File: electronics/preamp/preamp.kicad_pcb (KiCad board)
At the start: 2 copper layers, 33 parts, among them J1 Conn_01x01, J2 Conn_01x01, J3 Conn_01x01, J4 Conn_01x01, J5 Conn_01x01, J6 Conn_01x01, J7 Conn_01x01, Q1 BSS138L, U1 TL062, U2 TL062

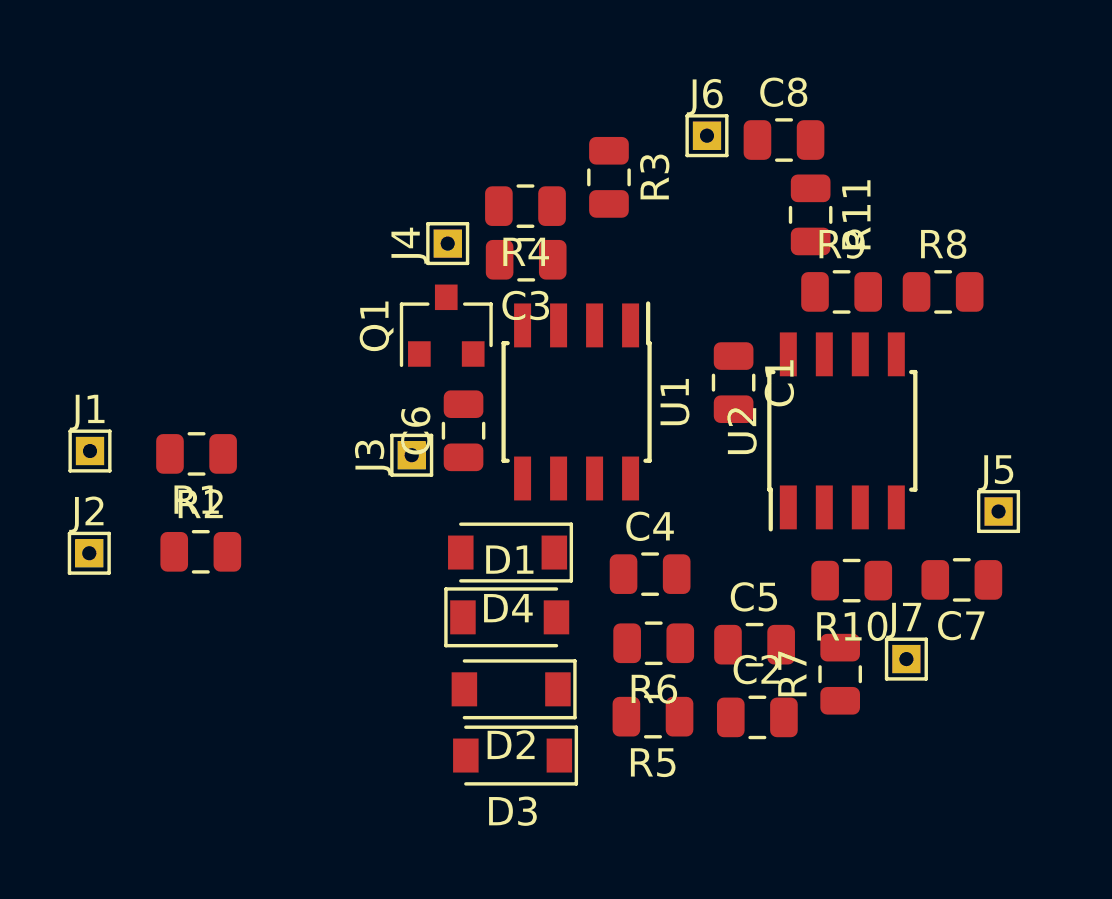
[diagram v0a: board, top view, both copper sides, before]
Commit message: Tweak component placement
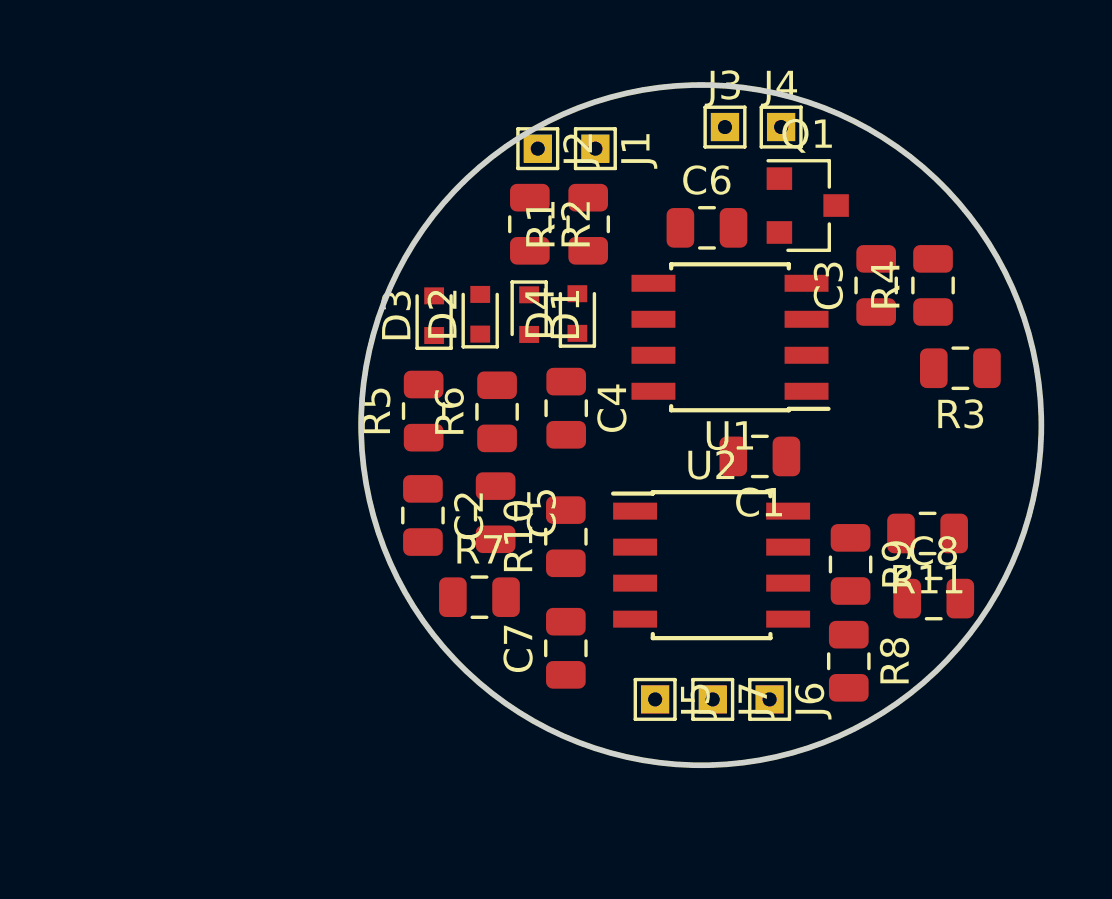
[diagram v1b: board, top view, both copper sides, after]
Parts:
- D1, D2, D3, D4: footprint Diode_SMD:D_SOD-123 -> Diode_SMD:D_SOD-523
- moved J2 21.3 mm to (94.2, 90.2), turned to 270 degrees
- moved J1 20.8 mm to (96.3, 90.2), turned to 270 degrees
- moved J6 20.0 mm to (102.4, 109.7), turned to 270 degrees
- moved C8 17.0 mm to (108.2, 106.1)
- moved R2 16.4 mm to (94.0, 92.9), turned to 270 degrees
- moved R1 16.0 mm to (96.0, 92.9), turned to 90 degrees
- moved J3 16.0 mm to (100.8, 89.5), turned to 0 degrees
- moved D3 15.8 mm to (90.6, 96.1), turned to 90 degrees
- moved R4 14.6 mm to (108.2, 95.1), turned to 90 degrees
- moved C7 14.2 mm to (95.2, 107.9), turned to 90 degrees
- moved R3 14.1 mm to (109.1, 98.0), turned to 180 degrees
- moved J5 13.8 mm to (98.4, 109.7), turned to 270 degrees
- moved C2 13.8 mm to (90.2, 103.2), turned to 270 degrees
- moved R5 13.5 mm to (90.2, 99.5), turned to 90 degrees
- moved R8 13.4 mm to (105.2, 108.3), turned to 270 degrees
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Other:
- board outline added: 24 x 24 mm
- board text added: "IN"
- board text added: "OUT"
- board text added: "PWR"

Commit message: Initial routing
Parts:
- C4: value 220pF -> 4.7pF
- R5: value 2k -> 22k
- R6: value 22k -> 220k
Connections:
- net Net-(R10-Pad2) renamed /BUF+
- net Net-(R11-Pad2) renamed /BUF-
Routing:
- net VGND: track 0.00 -> 52.4 mm, vias 0 -> 2
- net +BATT: track 0.00 -> 33.1 mm, vias 0 -> 2
- net GND: track 0.00 -> 26.9 mm
- net /BUF+: track 0.00 -> 21.0 mm, vias 0 -> 2
- net AMP: track 0.00 -> 20.8 mm, vias 0 -> 2
- net /PRE-: track 0.00 -> 12.9 mm
- net Net-(C4-Pad2): track 0.00 -> 9.68 mm
- net /PRE+: track 0.00 -> 7.73 mm
- net /OUT-: track 0.00 -> 7.35 mm
- net Net-(C3-Pad1): track 0.00 -> 6.56 mm
- net /BUF-: track 0.00 -> 4.18 mm
- net -BATT: track 0.00 -> 4.01 mm
- net Net-(R8-Pad1): track 0.00 -> 3.88 mm
- net /OUT+: track 0.00 -> 3.51 mm
- net Net-(C8-Pad2): track 0.00 -> 2.39 mm
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
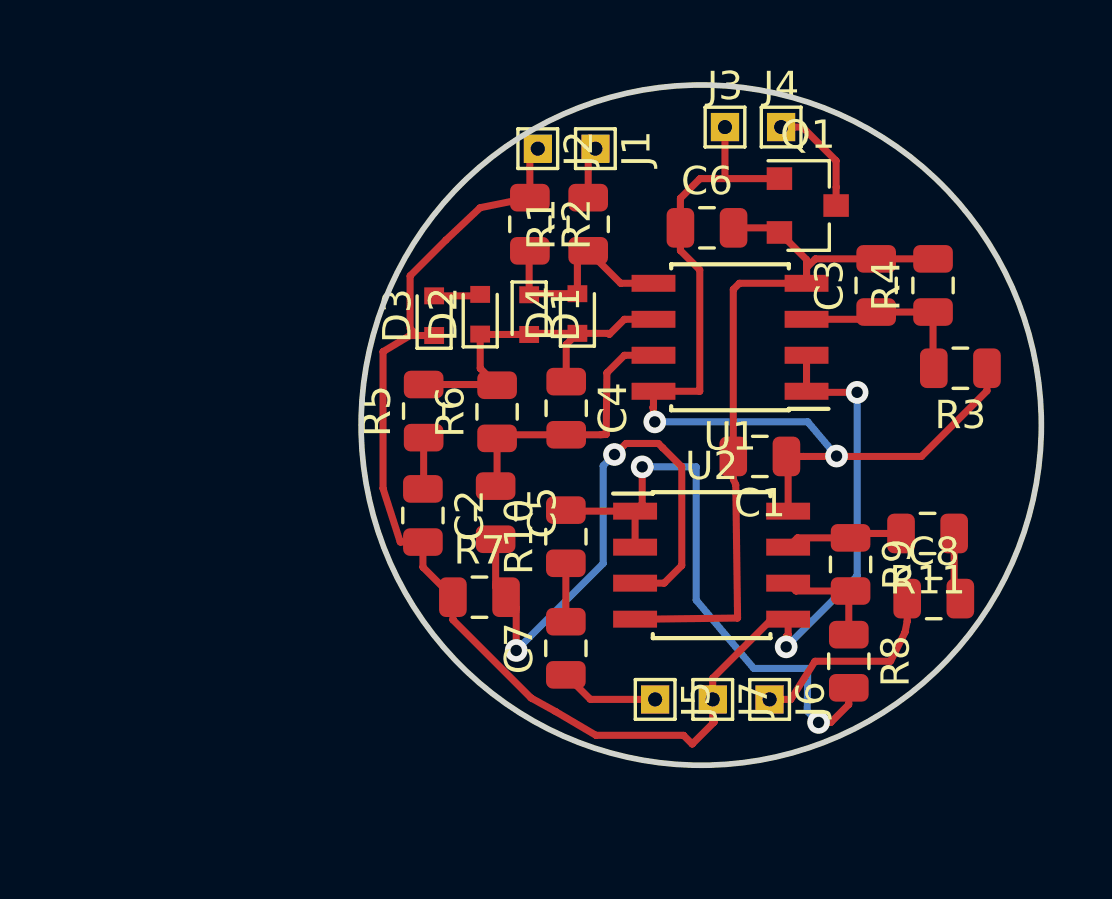
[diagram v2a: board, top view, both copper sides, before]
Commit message: Tweak routing a little bit
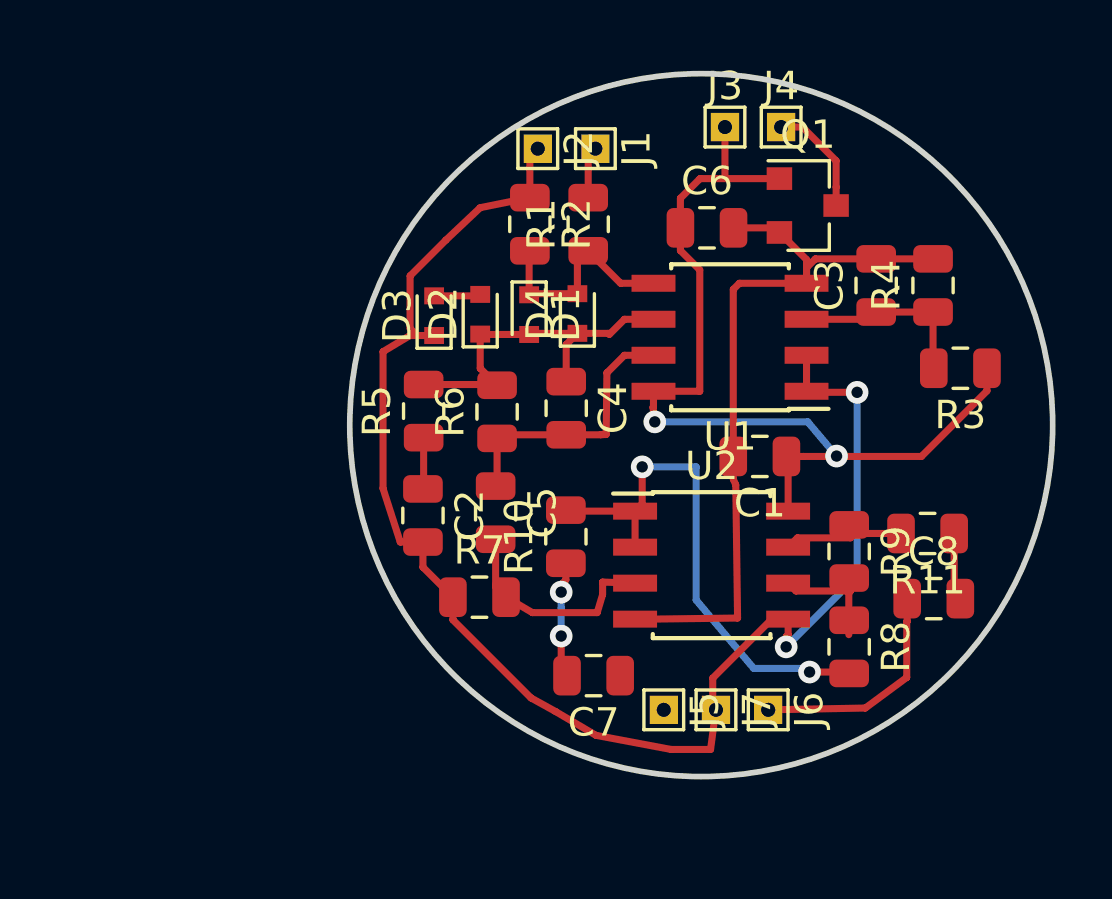
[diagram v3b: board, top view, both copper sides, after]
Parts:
- moved C7 1.37 mm to (96.2, 108.8), turned to 180 degrees
- moved R8 0.51 mm to (105.2, 107.8)
- moved J5 0.48 mm to (98.7, 110.0)
- moved R9 0.46 mm to (105.2, 104.5)
- moved J7 0.39 mm to (100.5, 110.0)
- moved J6 0.37 mm to (102.4, 110.0)
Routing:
- net AMP: track 20.8 -> 7.82 mm, vias 2 -> 0
- net /OUT+: track 3.51 -> 0.00 mm
- net /BUF+: track 21.0 -> 18.5 mm
- net Net-(C7-Pad2): track 2.06 -> 4.12 mm, vias 0 -> 2
- net /OUT-: track 7.35 -> 8.03 mm
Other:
- board size 24 x 24 mm -> 24.8 x 24.8 mm

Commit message: Ready to make first proto
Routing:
- net /OUT+: track 0.00 -> 2.04 mm
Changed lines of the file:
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@@
     (thickness 1.6)
     (drawings 4)
-    (tracks 165)
+    (tracks 166)
     (zones 0)
     (modules 33)
@@
     (tags SOT-23)
     (attr smd)
-    (fp_text reference Q1 (at 0 -2.5) (layer F.SilkS)
+    (fp_text reference Q1 (at 2.8575 -0.9398) (layer F.SilkS)
       (effects (font (size 1 1) (thickness 0.15)))
     )
@@
     (pad 1 smd roundrect (at -0.9375 0 90) (size 0.975 1.4) (layers F.Cu F.Paste F.Mask) (roundrect_rratio 0.25)
       (net 17 /PRE+))
-    (model ${KISYS3DMOD}/Resistor_SMD.3dshapes/R_0805_2012Metric.wrl
+    (model ${KISYS3DMOD}/Resistors_SMD.3dshapes/R_0805.wrl
       (at (xyz 0 0 0))
       (scale (xyz 1 1 1))
@@
     (tags "test point THT pad rectangle square")
     (attr virtual)
-    (fp_text reference J3 (at 0 -1.448) (layer F.SilkS)
+    (fp_text reference J3 (at -2.032 -0.2667) (layer F.SilkS)
       (effects (font (size 1 1) (thickness 0.15)))
     )
@@
     (tags "test point THT pad rectangle square")
     (attr virtual)
-    (fp_text reference J4 (at 0 -1.448) (layer F.SilkS)
+    (fp_text reference J4 (at 2.0828 -0.1397) (layer F.SilkS)
       (effects (font (size 1 1) (thickness 0.15)))
     )
@@
     )
   )
-  (gr_text OUT (at 104.4448 113.665) (layer Eco1.User)
+  (gr_text OUT (at 100.9015 112.5855) (layer Eco1.User)
     (effects (font (size 1.5 1.5) (thickness 0.3)))
   )
-  (gr_text PWR (at 106.0704 87.0712) (layer Eco1.User)
+  (gr_text PWR (at 102.235 86.36) (layer Eco1.User)
     (effects (font (size 1.5 1.5) (thickness 0.3)))
   )
-  (gr_text IN (at 90.9828 87.7316) (layer Eco1.User)
+  (gr_text IN (at 94.996 87.757) (layer Eco1.User)
     (effects (font (size 1.5 1.5) (thickness 0.3)))
   )
@@
   (segment (start 97.666657 105.575618) (end 96.52 105.537) (width 0.25) (layer F.Cu) (net 7))
   (segment (start 96.52 105.537) (end 96.52 105.9815) (width 0.25) (layer F.Cu) (net 7))
+  (segment (start 98.3465 110.0455) (end 97.14 108.839) (width 0.25) (layer F.Cu) (net 8))
+  (segment (start 98.679 110.0455) (end 98.3465 110.0455) (width 0.25) (layer F.Cu) (net 8))
   (segment (start 95.2246 105.4618) (end 95.0595 105.6269) (width 0.25) (layer F.Cu) (net 9))
   (segment (start 95.2246 104.8743) (end 95.2246 105.4618) (width 0.25) (layer F.Cu) (net 9))
@@
   (segment (start 104.759 91.6028) (end 104.759 92.2528) (width 0.25) (layer F.Cu) (net 14))
   (segment (start 102.8192 89.4842) (end 103.5692 89.4842) (width 0.25) (layer F.Cu) (net 14))
-  (segment (start 103.343757 105.852718) (end 103.066657 105.575618) (width 0.25) (layer F.Cu) (net 15))
-  (segment (start 105.268857 105.852718) (end 103.343757 105.852718) (width 0.25) (layer F.Cu) (net 15))
-  (segment (start 105.2068 105.914775) (end 105.268857 105.852718) (width 0.25) (layer F.Cu) (net 15))
-  (segment (start 105.2068 107.3935) (end 105.2068 105.914775) (width 0.25) (layer F.Cu) (net 15))
+  (segment (start 105.2195 106.8855) (end 105.2195 105.395) (width 0.25) (layer F.Cu) (net 15))
+  (segment (start 103.247275 105.395) (end 103.066657 105.575618) (width 0.25) (layer F.Cu) (net 15))
+  (segment (start 105.2195 105.395) (end 103.247275 105.395) (width 0.25) (layer F.Cu) (net 15))
   (segment (start 97.666657 103.035618) (end 97.666657 104.305618) (width 0.25) (layer F.Cu) (net 18))
   (segment (start 95.260918 103.035618) (end 95.2246 102.9993) (width 0.25) (layer F.Cu) (net 18))
